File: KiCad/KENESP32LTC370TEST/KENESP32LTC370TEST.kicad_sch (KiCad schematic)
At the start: 23 parts, among them J1 Test Point 10x Header, U1 LTC3780EUH-TRPBF

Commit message: Finished Schematic
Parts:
- added C1, C2, C3: 10u 35V, symbol Device:C_Small
- added C22, C4: .22u 16V, symbol Device:C_Small
- added C24: 1n, symbol Device:C_Small
- added C5, C6, C9: 22u 16V, symbol Device:C_Small
- added D3: 36V Zener, symbol Device:D_Zener
- added D4, D6, D7: B0540W, symbol Device:D_Schottky
- added D5: 1N5819HW, symbol Device:D_Schottky
- added L1: 10u, symbol Device:L
- added R19: 25m 2%, symbol Device:R_Small
- added R24, R26: 0, symbol Device:R_Small_US
- added R25: 1, symbol Device:R_Small_US
- added R8: 10, symbol Device:R_Small_US
- C18: renamed from C1; value 4.7u -> 4.7u Low ESR
- J1: value Test Point 10x Header -> Header Pins
- Q1: renamed from MOSFET1; value BSC009NE2LS5IATMA1 -> BSC009NE2LS5IATMA1 A (TG2)(1A)(BUCK)
- Q2: renamed from MOSFET2; value BSC009NE2LS5IATMA1 -> BSC009NE2LS5IATMA1 B (BG2)(1B)(BUCK)
- Q3: renamed from MOSFET3; value BSC009NE2LS5IATMA1 -> BSC009NE2LS5IATMA1 C (BG1)(2A)(BOOST)
- Q4: renamed from MOSFET4; value BSC009NE2LS5IATMA1 -> BSC009NE2LS5IATMA1 D (TG1)(2B)(BOOST)
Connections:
- net +6V: now also J1.8 (Pin_8), D4.2 (A), D7.2 (A)
- net EXTVCC: now also J1.1 (Pin_1); no longer J1.8 (Pin_8)
- net GND: now also U1.2 (SENSE-), U1.33 (EPAD), C1.1, C2.1, C24.1, C3.1, C5.1, C6.1, C9.1, D3.2 (A), R19.2; no longer J1.1 (Pin_1)
- net RUN: now also J1.5 (Pin_5)
- net VIN: now also Q1.5, Q1.6, Q1.7, Q1.8, C1.2, C2.2, C3.2, D3.1 (K)
- net VOS+: now also R8.2
- net VOUT: now also Q4.5, Q4.6, Q4.7, Q4.8, C5.2, C6.2, C9.2, D5.1 (K), R8.1
- net SW2: now reaches Q1.1
- net SW2: now also Q1.2, Q1.3, Q2.5, Q2.6, Q2.7, Q2.8, U1.17 (SW2), C22.2, D6.1 (K), L1.1, R25.2
- net TG2: now reaches Q1.4
- net TG2: now also U1.15 (TG2)
- net SENSE+: now reaches U1.1 (SENSE+)
- net SENSE+: now also J1.9 (Pin_9), Q2.1, Q2.2, Q2.3, Q3.1, Q3.2, Q3.3, D6.2 (A), R19.1
- net BOOST2: now reaches U1.14 (BOOST2)
- net BOOST2: now also R26.1
- net BG2: now reaches U1.18 (BG2)
- net BG2: now also Q2.4
- net BG1: now reaches U1.20 (BG1)
- net BG1: now also Q3.4
- net SW1: now reaches U1.24 (SW1)
- net SW1: now also Q3.5, Q3.6, Q3.7, Q3.8, Q4.1, Q4.2, Q4.3, C4.2, D5.2 (A), L1.2
- net TG1: now reaches U1.26 (TG1)
- net TG1: now also Q4.4
- net BOOST1: now reaches U1.27 (BOOST1)
- net BOOST1: now also R24.1
- new net: C22.1, D7.1 (K), R26.2
- new net: C4.1, D4.1 (K), R24.2
- new net: C24.2, R25.1
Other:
- note added: "Boosted Floating Driver Supply"
- note added: "Bottom Gate Drivers"
- note added: "Bypass / Filter Capacitors"
- note added: "Control / Test Header"
- note added: "Current Sense Feedback"
- note added: "Input Stage"
- note added: "LTC3780 IC"
- note added: "Output Stage"
- note added: "Output Switching Power Circuit"
- note added: "Overvoltage Protection"
- note added: "Top Gate Drivers"
- note added: "Voltage Feedback"
- title: (none) -> LTC3780 Development Circuit
- moved on the sheet: C10, C12, C13, C15, C18, C19, C21, C23, CC14, D1, J1, Q1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

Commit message: fixed errors. need footprints and PCB layout
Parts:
- removed R19: 25m 2%, symbol Device:R_Small
- added C11: 68p, symbol Device:C_Small
- added R1: 25m 2%, symbol Device:R_Small
- added R10, R9: 100 1%, symbol Device:R_Small_US
- added R5: 10, symbol Device:R_Small_US
- renumbered CC14 to C14
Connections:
- net GND: now also R1.2, R10.2; no longer U1.2 (SENSE-)
- net SENSE+: now also C11.2, R9.1; no longer D6.2 (A), Q2.1, Q2.2, Q2.3, Q3.1, Q3.2, Q3.3
- net VIN: now also R5.2; no longer C1.2, C2.2, C3.2
- new net: C1.2, C2.2, C3.2, R5.1
- new net SENSE-: C11.1, R10.1, U1.2 (SENSE-)
- new net SHUNT+: D6.2 (A), Q2.1, Q2.2, Q2.3, Q3.1, Q3.2, Q3.3, R1.1, R9.2

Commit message: PCB Layout Started
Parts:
- C1, C10, C11, C12, C13, C14, C15, C19, C2, C21, C22, C23, C24, C3, C4, C5, C6, C9: footprint (none) -> Capacitor_SMD:C_1206_3216Metric_Pad1.33x1.80mm_HandSolder
- C18: footprint (none) -> Mechatronic Footprints:LOWESRCAPMP7.6X4.3_3.1N_KEM
- D1, D3: footprint (none) -> Diode_SMD:D_SOD-123
- D4, D5, D6, D7: footprint (none) -> Mechatronic Footprints:CR_SMA_320-340AE_DIO
- J1: footprint (none) -> Connector_PinHeader_2.54mm:PinHeader_1x10_P2.54mm_Vertical
- L1: footprint (none) -> Mechatronic Footprints:IND_410680_WRE
- Q1, Q2, Q3, Q4: footprint PG-TDSON-8_INF -> Mechatronic Footprints:PG-TDSON-8_INF
- R10, R11, R12, R13, R15, R20, R23, R24, R25, R5, R7, R8, R9: footprint (none) -> Resistor_SMD:R_1206_3216Metric_Pad1.30x1.75mm_HandSolder
- R19: renamed from R1; footprint (none) -> Resistor_SMD:R_1206_3216Metric_Pad1.30x1.75mm_HandSolder
- R26: footprint (none) -> Resistor_SMD:R_1210_3225Metric_Pad1.30x2.65mm_HandSolder
- U1: footprint QFN-32_UH_LIT -> Mechatronic Footprints:QFN-32_UH_LIT
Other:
- note added: "LTC3780EUH Development Circuit"
- note removed: "LTC3780EUH DEMO CIRCUIT 1155A by KISHIO"

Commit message: PCB Layout Continued
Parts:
- R26: footprint Resistor_SMD:R_1210_3225Metric_Pad1.30x2.65mm_HandSolder -> Resistor_SMD:R_1206_3216Metric_Pad1.30x1.75mm_HandSolder
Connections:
- net VIN: now also C1.2, C2.2, C3.2, R5.1; no longer D3.1 (K), R5.2, U1.23 (VIN)
- new net VCC: D3.1 (K), R5.2, U1.23 (VIN)
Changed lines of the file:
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@@
     (fill (type none))
   )
-  (rectangle (start 244.602 78.994) (end 305.308 95.758)
+  (rectangle (start 244.602 77.978) (end 305.308 95.758)
     (stroke (width 0) (type default))
     (fill (type none))
@@
     (effects (font (size 3 3)) (justify left bottom))
   )
-  (text "Input Stage" (at 260.604 77.47 0)
+  (text "Input Stage" (at 260.35 76.708 0)
     (effects (font (size 3 3)) (justify left bottom))
   )
@@
     )
   )
-  (global_label "VIN" (shape input) (at 227.584 117.094 0) (fields_autoplaced)
-    (effects (font (size 1.27 1.27)) (justify left))
-    (property "Intersheetrefs" "${INTERSHEET_REFS}" (at 233.5137 117.094 0)
-      (effects (font (size 1.27 1.27)) (justify left) hide)
+  (global_label "VCC" (shape input) (at 227.584 117.094 0) (fields_autoplaced)
+    (effects (font (size 1.27 1.27)) (justify left))
+    (property "Intersheetrefs" "${INTERSHEET_REFS}" (at 234.1184 117.094 0)
+      (effects (font (size 1.27 1.27)) (justify left) hide)
+    )
+  )
+  (global_label "VCC" (shape input) (at 252.476 81.026 180) (fields_autoplaced)
+    (effects (font (size 1.27 1.27)) (justify right))
+    (property "Intersheetrefs" "${INTERSHEET_REFS}" (at 245.9416 81.026 0)
+      (effects (font (size 1.27 1.27)) (justify right) hide)
     )
   )
@@
     )
   )
+  (global_label "VIN" (shape input) (at 293.878 81.026 0) (fields_autoplaced)
+    (effects (font (size 1.27 1.27)) (justify left))
+    (property "Intersheetrefs" "${INTERSHEET_REFS}" (at 299.8077 81.026 0)
+      (effects (font (size 1.27 1.27)) (justify left) hide)
+    )
+  )
   (global_label "SW2" (shape input) (at 122.428 185.42 180) (fields_autoplaced)
     (effects (font (size 1.27 1.27)) (justify right))
@@
     (effects (font (size 1.27 1.27)) (justify right))
     (property "Intersheetrefs" "${INTERSHEET_REFS}" (at 307.8692 84.582 0)
-      (effects (font (size 1.27 1.27)) (justify right) hide)
-    )
-  )
-  (global_label "VIN" (shape input) (at 252.476 81.026 180) (fields_autoplaced)
-    (effects (font (size 1.27 1.27)) (justify right))
-    (property "Intersheetrefs" "${INTERSHEET_REFS}" (at 246.5463 81.026 0)
       (effects (font (size 1.27 1.27)) (justify right) hide)
     )
@@
       (effects (font (size 1.27 1.27)))
     )
-    (property "Footprint" "Resistor_SMD:R_1210_3225Metric_Pad1.30x2.65mm_HandSolder" (at 229.108 196.596 0)
+    (property "Footprint" "Resistor_SMD:R_1206_3216Metric_Pad1.30x1.75mm_HandSolder" (at 229.108 196.596 0)
       (effects (font (size 1.27 1.27)) hide)
     )
@@
   (symbol (lib_id "Device:C_Small") (at 293.878 83.566 180) (unit 1)
     (in_bom yes) (on_board yes) (dnp no)
-    (property "Reference" "C3" (at 297.688 82.55 0)
-      (effects (font (size 1.27 1.27)))
-    )
-    (property "Value" "10u 35V" (at 300.228 84.582 0)
-      (effects (font (size 1.27 1.27)))
-    )
+    (property "Reference" "C3" (at 297.434 84.074 0)
+      (effects (font (size 1.27 1.27)))
+    )
+    (property "Value" "10u 35V" (at 299.72 86.106 0)
+      (effects (font (size 1.27 1.27)))
+    )

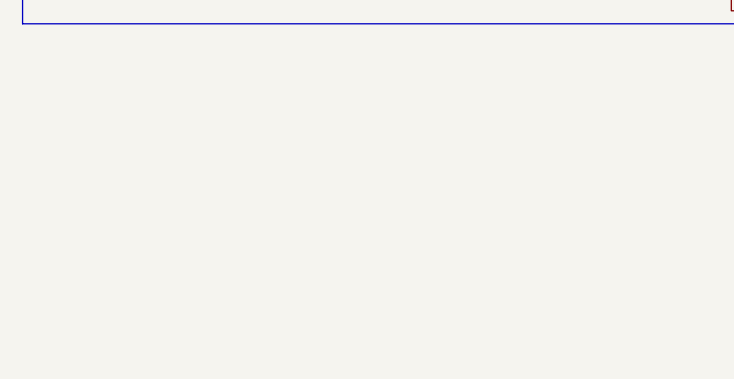
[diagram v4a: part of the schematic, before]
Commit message: LTC3780 Completed. PCB Ordered
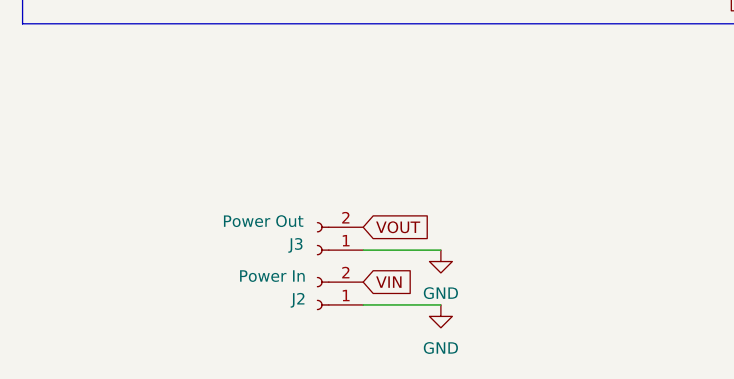
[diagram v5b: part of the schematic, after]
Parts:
- added J2: Power In, Connector_AMASS:AMASS_XT30U-M_1x02_P5.0mm_Vertical, symbol Connector:Conn_01x02_Socket
- added J3: Power Out, Connector_AMASS:AMASS_XT30U-F_1x02_P5.0mm_Vertical, symbol Connector:Conn_01x02_Socket
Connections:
- net GND: now also J2.1 (Pin_1), J3.1 (Pin_1)
- net VIN: now also J2.2 (Pin_2)
- net VOUT: now also J3.2 (Pin_2)
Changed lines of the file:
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@@
+    (stroke (width 0) (type default))
+  )
+  (wire (pts (xy 86.36 250.698) (xy 94.996 250.698))
     (stroke (width 0) (type default))
   )
@@
   )
   (wire (pts (xy 134.874 185.42) (xy 134.874 197.104))
+    (stroke (width 0) (type default))
+  )
+  (wire (pts (xy 86.36 256.794) (xy 94.996 256.794))
     (stroke (width 0) (type default))
   )
@@
     )
   )
+  (global_label "VOUT" (shape input) (at 86.36 248.158 0) (fields_autoplaced)
+    (effects (font (size 1.27 1.27)) (justify left))
+    (property "Intersheetrefs" "${INTERSHEET_REFS}" (at 93.983 248.158 0)
+      (effects (font (size 1.27 1.27)) (justify left) hide)
+    )
+  )
   (global_label "VOUT" (shape input) (at 149.352 175.006 90) (fields_autoplaced)
     (effects (font (size 1.27 1.27)) (justify left))
@@
     (property "Intersheetrefs" "${INTERSHEET_REFS}" (at 128.524 225.0228 90)
       (effects (font (size 1.27 1.27)) (justify right) hide)
+    )
+  )
+  (global_label "VIN" (shape input) (at 86.36 254.254 0) (fields_autoplaced)
+    (effects (font (size 1.27 1.27)) (justify left))
+    (property "Intersheetrefs" "${INTERSHEET_REFS}" (at 92.2897 254.254 0)
+      (effects (font (size 1.27 1.27)) (justify left) hide)
     )
   )
@@
     )
   )
+  (symbol (lib_id "power:GND") (at 94.996 256.794 0) (unit 1)
+    (in_bom yes) (on_board yes) (dnp no) (fields_autoplaced)
+    (property "Reference" "#PWR020" (at 94.996 263.144 0)
+      (effects (font (size 1.27 1.27)) hide)
+    )
+    (property "Value" "GND" (at 94.996 261.62 0)
+      (effects (font (size 1.27 1.27)))
+    )
+    (property "Footprint" "" (at 94.996 256.794 0)
+      (effects (font (size 1.27 1.27)) hide)
+    )
+    (property "Datasheet" "" (at 94.996 256.794 0)
+      (effects (font (size 1.27 1.27)) hide)
+    )
+    (pin "1")
+    (instances
+      (project "KENESP32LTC370TEST"
+        (path "/5e9cfb74-656a-48c0-8f94-6c53cb1501bf"
+          (reference "#PWR020") (unit 1)
+        )
+      )
+    )
+  )
   (symbol (lib_id "power:GND") (at 255.524 88.646 0) (unit 1)
     (in_bom yes) (on_board yes) (dnp no)
@@
         (path "/5e9cfb74-656a-48c0-8f94-6c53cb1501bf"
           (reference "#PWR07") (unit 1)
+        )
+      )
+    )
+  )
+  (symbol (lib_id "Connector:Conn_01x02_Socket") (at 81.28 256.794 180) (unit 1)
+    (in_bom yes) (on_board yes) (dnp no) (fields_autoplaced)
+    (property "Reference" "J2" (at 80.01 256.159 0)
+      (effects (font (size 1.27 1.27)) (justify left))
+    )
+    (property "Value" "Power In" (at 80.01 253.619 0)
+      (effects (font (size 1.27 1.27)) (justify left))
+    )
+    (property "Footprint" "Connector_AMASS:AMASS_XT30U-M_1x02_P5.0mm_Vertical" (at 81.28 256.794 0)
+      (effects (font (size 1.27 1.27)) hide)
+    )
+    (property "Datasheet" "~" (at 81.28 256.794 0)
+      (effects (font (size 1.27 1.27)) hide)
+    )
+    (pin "1")
+    (pin "2")
+    (instances
+      (project "KENESP32LTC370TEST"
+        (path "/5e9cfb74-656a-48c0-8f94-6c53cb1501bf"
+          (reference "J2") (unit 1)
         )
       )
@@
     )
   )
+  (symbol (lib_id "power:GND") (at 94.996 250.698 0) (unit 1)
+    (in_bom yes) (on_board yes) (dnp no) (fields_autoplaced)
+    (property "Reference" "#PWR028" (at 94.996 257.048 0)
+      (effects (font (size 1.27 1.27)) hide)
+    )
+    (property "Value" "GND" (at 94.996 255.524 0)
+      (effects (font (size 1.27 1.27)))
+    )
+    (property "Footprint" "" (at 94.996 250.698 0)
+      (effects (font (size 1.27 1.27)) hide)
+    )
+    (property "Datasheet" "" (at 94.996 250.698 0)
+      (effects (font (size 1.27 1.27)) hide)
+    )
+    (pin "1")
+    (instances
+      (project "KENESP32LTC370TEST"
+        (path "/5e9cfb74-656a-48c0-8f94-6c53cb1501bf"
+          (reference "#PWR028") (unit 1)
+        )
+      )
+    )
+  )
   (symbol (lib_id "power:GND") (at 59.436 92.964 270) (unit 1)
     (in_bom yes) (on_board yes) (dnp no)
@@
         )
       )
+    )
+  )
+  (symbol (lib_id "Connector:Conn_01x02_Socket") (at 81.28 250.698 180) (unit 1)
+    (in_bom yes) (on_board yes) (dnp no) (fields_autoplaced)
+    (property "Reference" "J3" (at 79.756 250.063 0)
+      (effects (font (size 1.27 1.27)) (justify left))
+    )
+    (property "Value" "Power Out" (at 79.756 247.523 0)
+      (effects (font (size 1.27 1.27)) (justify left))
+    )
+    (property "Footprint" "Connector_AMASS:AMASS_XT30U-F_1x02_P5.0mm_Vertical" (at 81.28 250.698 0)
+      (effects (font (size 1.27 1.27)) hide)
+    )
+    (property "Datasheet" "~" (at 81.28 250.698 0)
+      (effects (font (size 1.27 1.27)) hide)
+    )
+    (pin "1")
+    (pin "2")
+    (instances
+      (project "KENESP32LTC370TEST"
+        (path "/5e9cfb74-656a-48c0-8f94-6c53cb1501bf"
+          (reference "J3") (unit 1)
+        )
+      )
